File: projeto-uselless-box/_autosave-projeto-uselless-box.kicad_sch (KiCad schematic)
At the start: 10 parts, among them J2 Conn_Para_Fita, M1 Motor_Servo, M2 Motor_Servo, M3 Motor_Servo, SW1 SW_DPST_x2

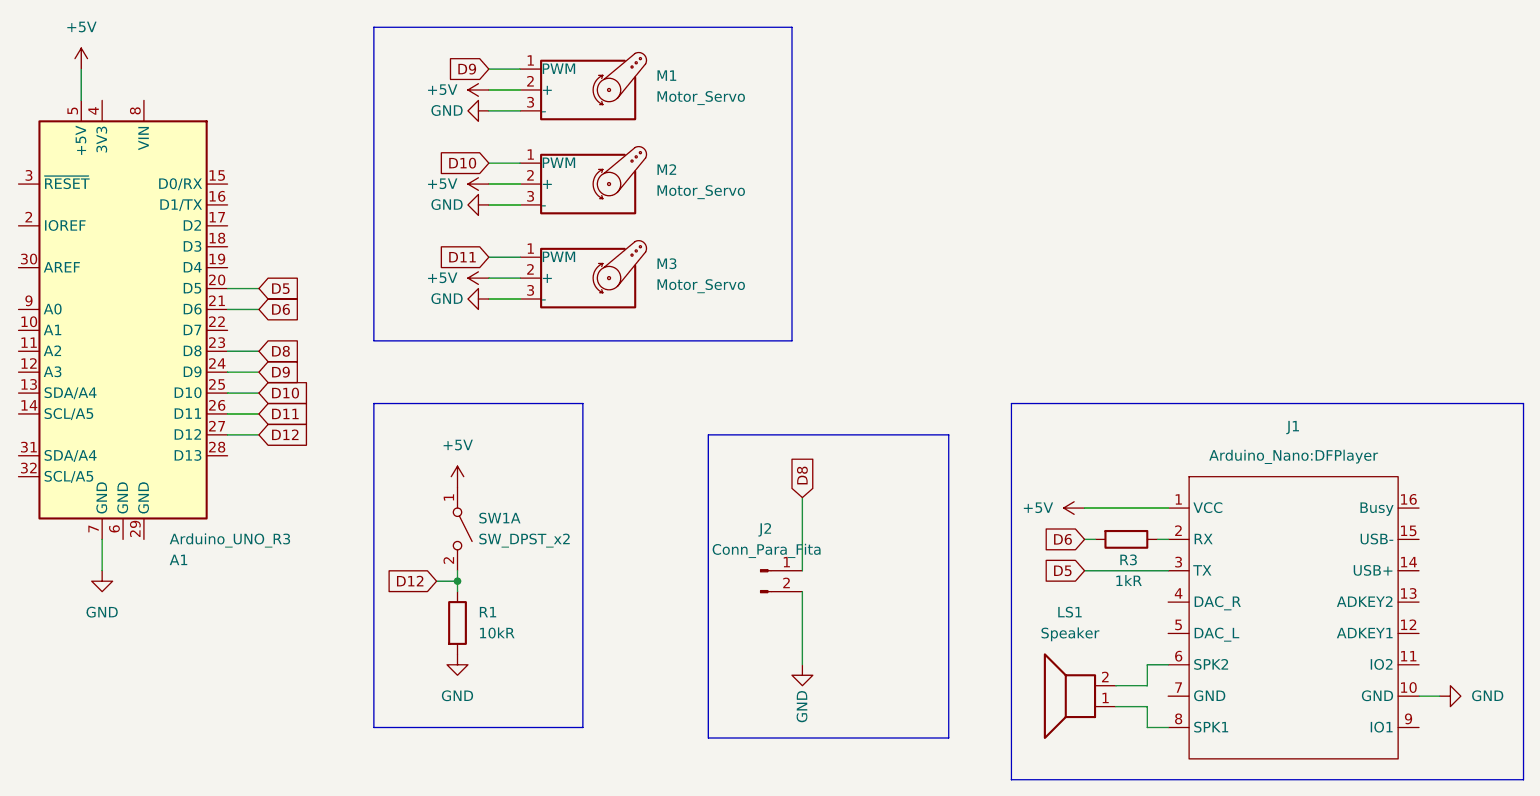
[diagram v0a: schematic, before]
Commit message: Working in the Transistor of LED strip
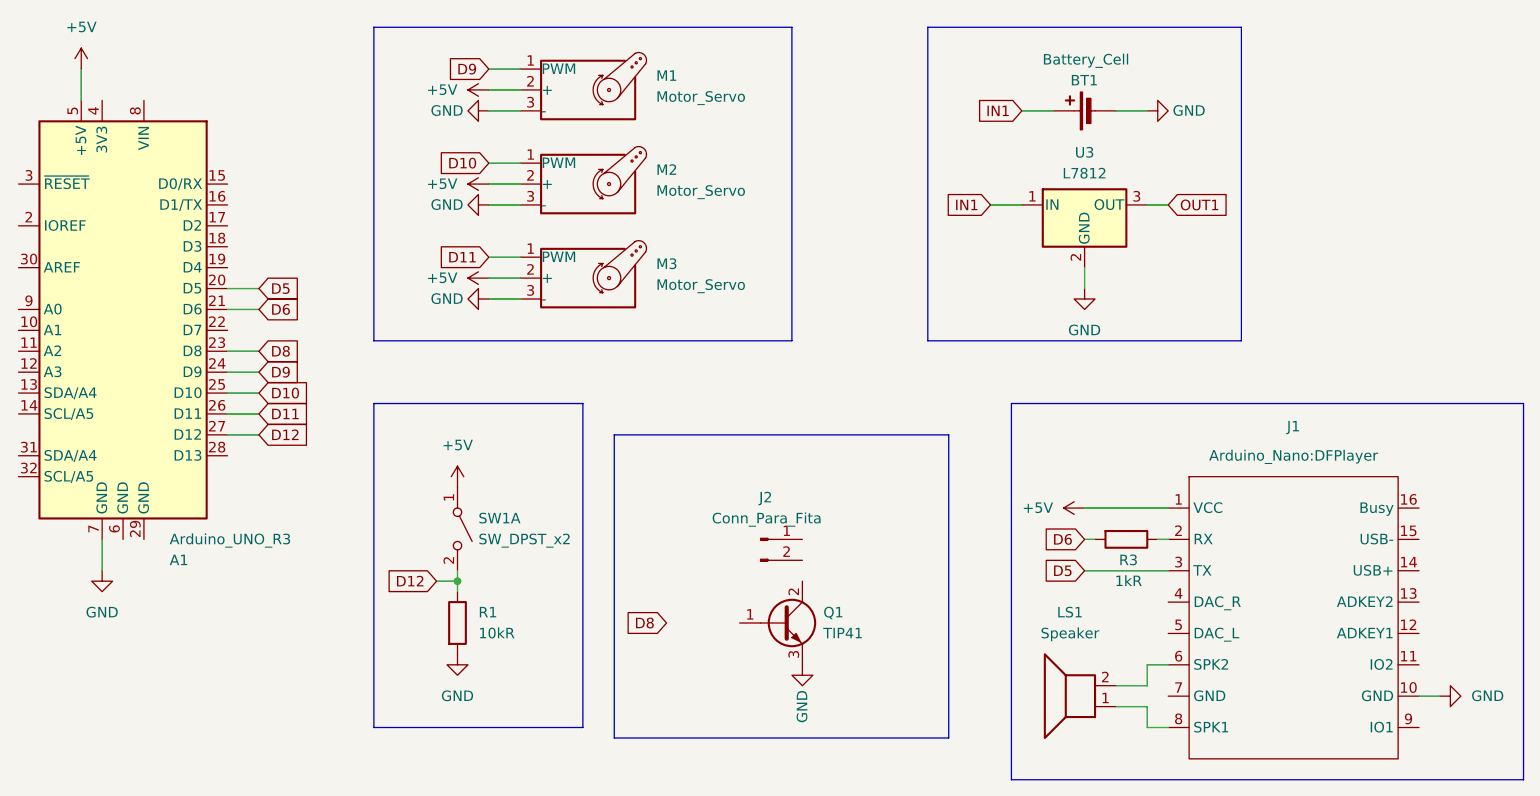
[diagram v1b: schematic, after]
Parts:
- added BT1: Battery_Cell, symbol Device:Battery_Cell
- added Q1: TIP41, Package_TO_SOT_THT:TO-220-3_Vertical, symbol Transistor_BJT:TIP41
- added U3: L7812, symbol Regulator_Linear:L7812
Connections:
- net D8: no longer J2.1 (Pin_1)
- net GND: now also BT1.2 (-), Q1.3 (E), U3.2 (GND); no longer J2.2 (Pin_2)
- new net IN1: BT1.1 (+), U3.1 (IN)
- new net OUT1: U3.3 (OUT)
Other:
- moved on the sheet: J2

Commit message: Finished the first prototype of PCB
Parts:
- removed BT1: Battery_Cell, symbol Device:Battery_Cell
- removed M1, M2, M3: Motor_Servo, Connector_PinSocket_2.54mm:PinSocket_1x03_P2.54mm_Vertical, symbol Motor:Motor_Servo
- removed U3: L7812, symbol Regulator_Linear:L7812
- added J3: Conn_Para_PowerBank, TerminalBlock_Phoenix:TerminalBlock_Phoenix_MKDS-1,5-2-5.08_1x02_P5.08mm_Horizontal, symbol Connector:Conn_01x02_Pin
- added M1, M2, M3: Motor_Servo-Edit, Connector_PinSocket_2.54mm:PinSocket_1x02_P2.54mm_Vertical, symbol New_Library:Motor_Servo-Edit
- added R2: 100R, Resistor_THT:R_Axial_DIN0207_L6.3mm_D2.5mm_P10.16mm_Horizontal, symbol Device:R
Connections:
- net +5V: now also M1.2 (+), M2.2 (+), M3.2 (+)
- net D10: now also M2.3 (PWM)
- net D11: now also M3.3 (PWM)
- net D8: now also R2.1
- net D9: now also M1.3 (PWM)
- net GND: now also J3.1 (Pin_1), M1.1 (-), M2.1 (-), M3.1 (-)
- net at Q1.1 (B): now also R2.2
- net at Q1.2 (C): now also J2.2 (Pin_2)
- net at J2.1 (Pin_1): now also J3.2 (Pin_2)
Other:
- moved on the sheet: J1, J2, LS1, Q1, R3
